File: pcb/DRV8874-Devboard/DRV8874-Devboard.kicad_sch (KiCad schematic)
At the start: 8 parts, among them J1 Conn_01x04_Pin, J2 Screw_Terminal_01x02, J3 Conn_01x03_Pin, U1 DRV8874

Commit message: updated BOM
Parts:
- added C5: 100nF, symbol Device:C
- added U2: TinyThinker_J1, Connector_PinSocket_2.54mm:PinSocket_2x20_P2.54mm_Vertical, symbol Custom_Library:TinyThinker_J1
- added U3: TinyThinker_J2, Connector_PinSocket_2.54mm:PinSocket_2x20_P2.54mm_Vertical, symbol Custom_Library:TinyThinker_J2
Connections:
- net +3.3V: now also U3.1 (+3.3V), U3.10 (+3.3V), U3.18 (+3.3V), U3.2 (+3.3V), U3.21 (+3.3V), U3.22 (+3.3V), U3.29 (+3.3V), U3.30 (+3.3V), U3.38 (+3.3V), U3.9 (+3.3V)
- net +BATT: now also C5.1
- net GND: now also C5.2, U3.16 (GND), U3.19 (GND), U3.20 (GND), U3.27 (GND), U3.28 (GND), U3.36 (GND), U3.39 (GND), U3.40 (GND), U3.7 (GND), U3.8 (GND)
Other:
- moved on the sheet: C1, C2, C3, C4, J3, U1

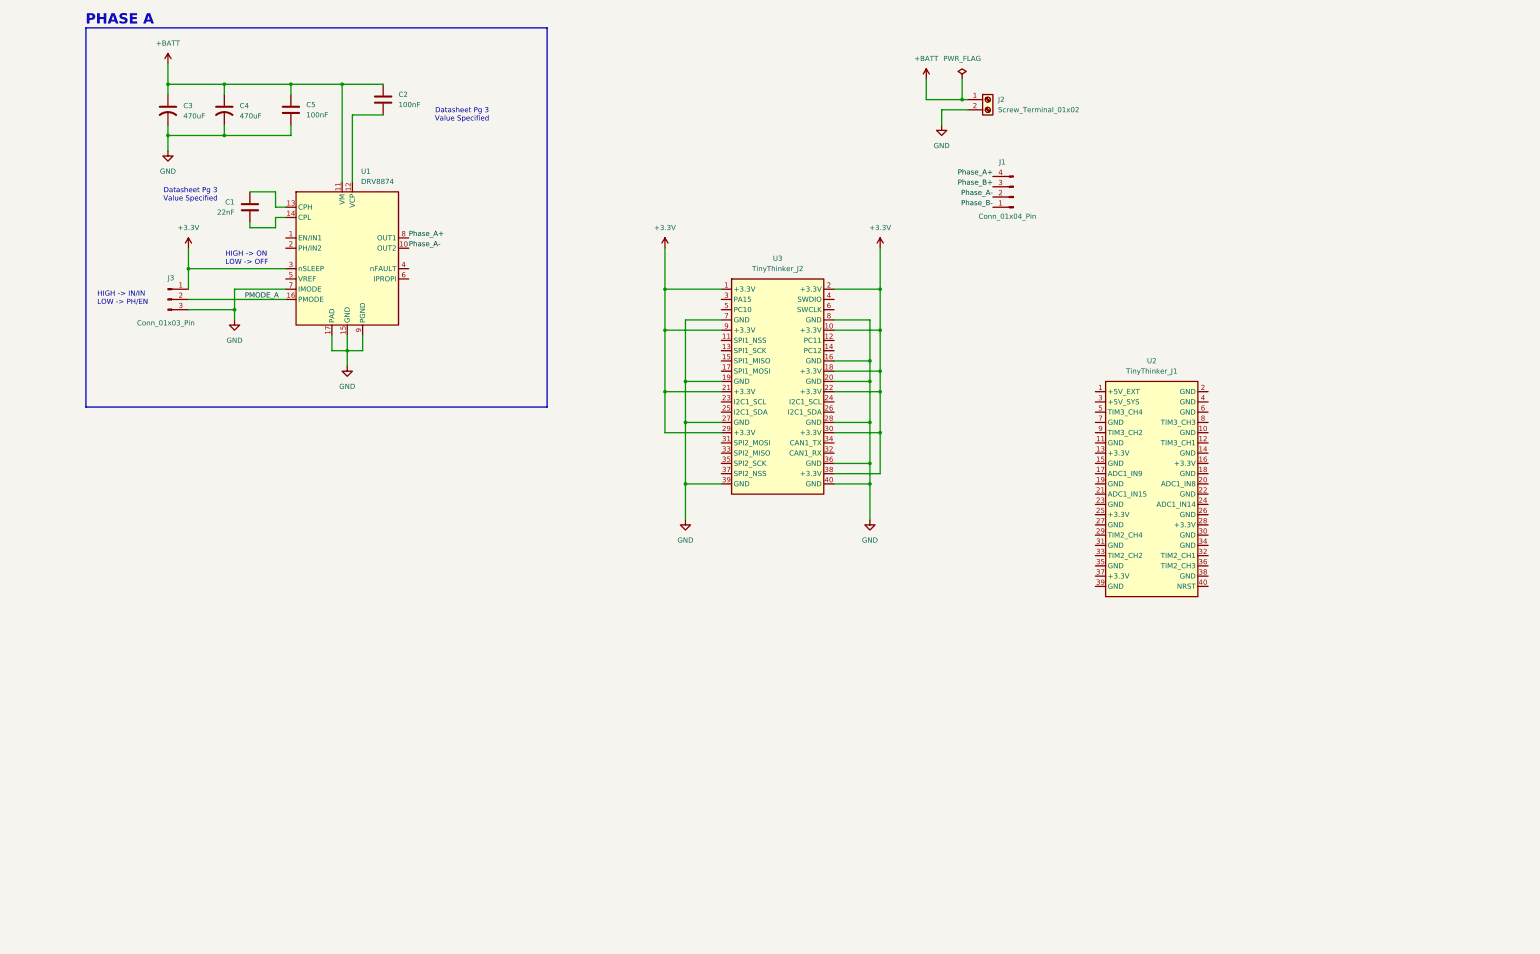
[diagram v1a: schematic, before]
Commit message: added CAN transciever
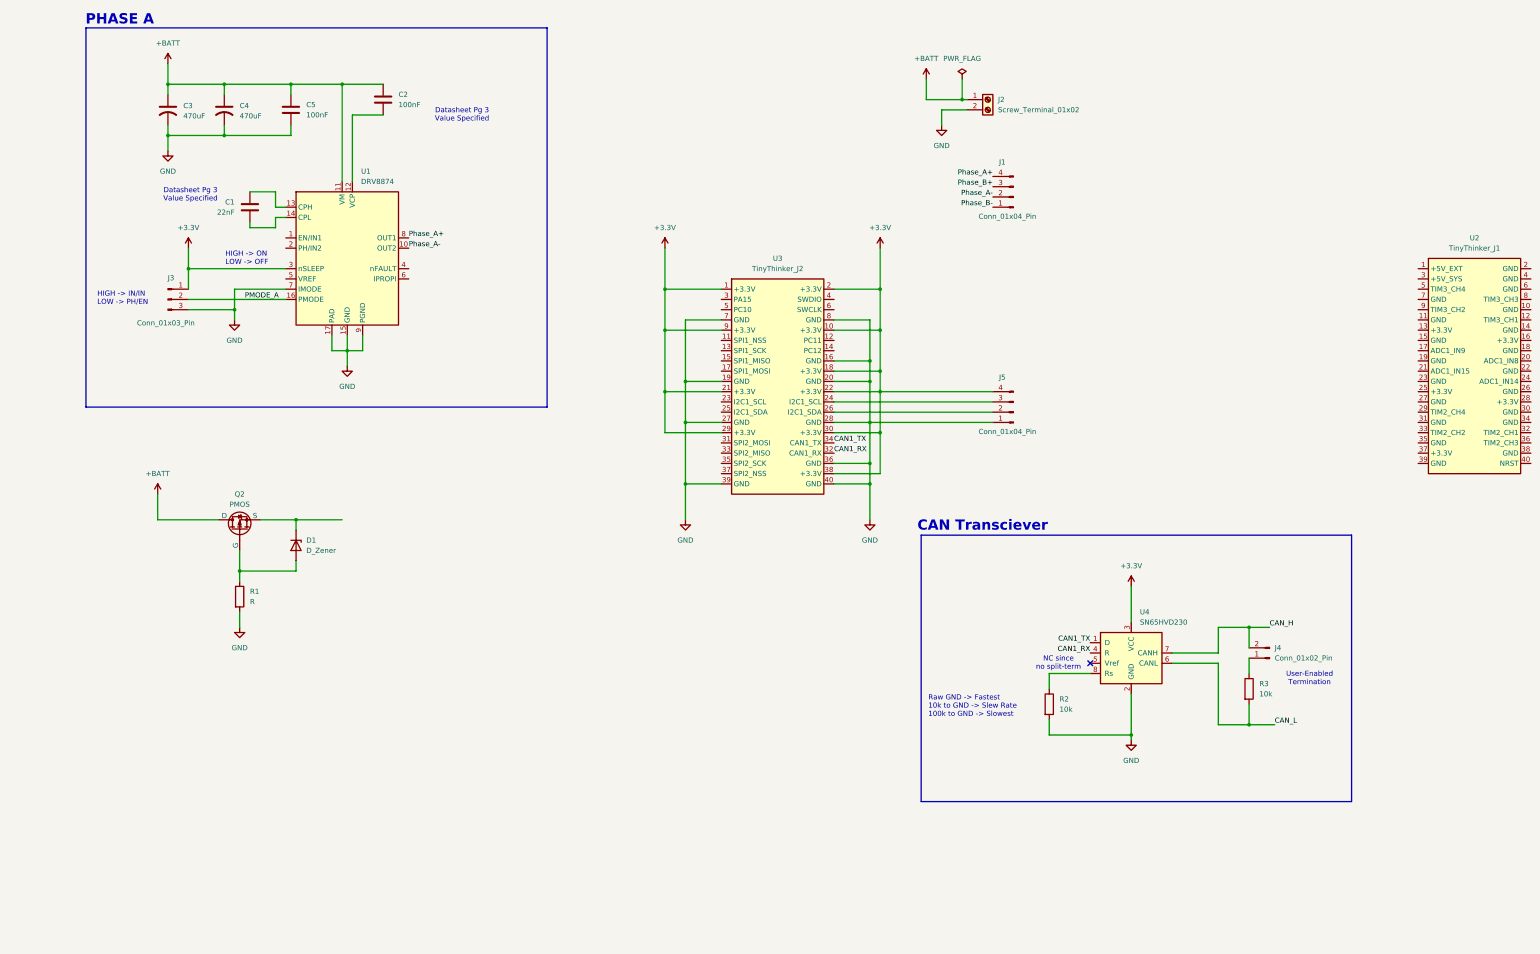
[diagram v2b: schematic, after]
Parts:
- added D1: D_Zener, symbol Device:D_Zener
- added J4: Conn_01x02_Pin, Connector_PinHeader_2.54mm:PinHeader_1x02_P2.54mm_Vertical, symbol Connector:Conn_01x02_Pin
- added J5: Conn_01x04_Pin, symbol Connector:Conn_01x04_Pin
- added Q2: PMOS, symbol Simulation_SPICE:PMOS
- added R1: R, symbol Device:R
- added R2, R3: 10k, symbol Device:R
- added U4: SN65HVD230, Package_SO:SOIC-8_3.9x4.9mm_P1.27mm, symbol Interface_CAN_LIN:SN65HVD230
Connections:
- net +3.3V: now also J5.4 (Pin_4), U4.3 (VCC)
- net +BATT: now also Q2.1 (D)
- net GND: now also J5.1 (Pin_1), R1.2, R2.2, U4.2 (GND)
- net at U3.24 (I2C1_SCL): now also J5.3 (Pin_3)
- net at U3.26 (I2C1_SDA): now also J5.2 (Pin_2)
- net CAN1_RX: now reaches U3.32 (CAN1_RX)
- net CAN1_RX: now also U4.4 (R)
- net CAN1_TX: now reaches U3.34 (CAN1_TX)
- net CAN1_TX: now also U4.1 (D)
- new net: J4.1 (Pin_1), R3.1
- new net: R2.1, U4.8 (Rs)
- new net: D1.2 (A), Q2.2 (G), R1.1
- new net: D1.1 (K), Q2.3 (S)
- new net CAN_H: J4.2 (Pin_2), U4.7 (CANH)
- new net CAN_L: R3.2, U4.6 (CANL)
- no-connect marks 0 -> 1
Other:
- note added: "CAN Transciever"
- note added: "NC since no split-term"
- note added: "Raw GND -> Fastest 10k to GND -> Slew Rate 100k to GND -> Slowest"
- note added: "User-Enabled Termination"
- moved on the sheet: U2

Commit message: exposed more connectors on DRV8874 devb
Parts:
- removed J4: Conn_01x02_Pin, Connector_PinHeader_2.54mm:PinHeader_1x02_P2.54mm_Vertical, symbol Connector:Conn_01x02_Pin
- added J4, J6, J7: Conn_01x03_Pin, Connector_PinHeader_2.54mm:PinHeader_1x03_P2.54mm_Vertical, symbol Connector:Conn_01x03_Pin
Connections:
- net CAN_H: now also J4.3 (Pin_3), J7.3 (Pin_3)
- net CAN_L: now also J7.1 (Pin_1)
- net GND: now also J6.1 (Pin_1), J7.2 (Pin_2)
- net I2C1_SDA: now reaches J5.2 (Pin_2), U3.26 (I2C1_SDA)
- net I2C1_SCL: now reaches J5.3 (Pin_3), U3.24 (I2C1_SCL)
- net at R3.1: now also J4.2 (Pin_2)
- net at U4.8 (Rs): now also J6.2 (Pin_2); no longer R2.1
- new net: J6.3 (Pin_3), R2.1
- no-connect marks 1 -> 4
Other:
- note added: "3 pin to hold jumper"
- note added: "CAN Connector"
- note added: "I2C Connector"
- note added: "Jumper to control speed"
- note added: "Stepper Connector"
- moved on the sheet: J1, R2, R3, U2, U4

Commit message: started working on drv8874
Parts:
- added U5: DRV8841PWP, DRV8841PWP:IC_TPS61196PWPRQ1, symbol DRV8841PWP:DRV8841PWP
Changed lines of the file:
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@@
+	)
+	(symbol
+		(lib_id "DRV8841PWP:DRV8841PWP")
+		(at 181.61 214.63 0)
+		(unit 1)
+		(exclude_from_sim no)
+		(in_bom yes)
+		(on_board yes)
+		(dnp no)
+		(fields_autoplaced yes)
+		(property "Reference" "U5"
+			(at 181.61 173.99 0)
+			(effects
+				(font
+					(size 1.27 1.27)
+				)
+			)
+		)
+		(property "Value" "DRV8841PWP"
+			(at 181.61 176.53 0)
+			(effects
+				(font
+					(size 1.27 1.27)
+				)
+			)
+		)
+		(property "Footprint" "DRV8841PWP:IC_TPS61196PWPRQ1"
+			(at 181.61 214.63 0)
+			(effects
+				(font
+					(size 1.27 1.27)
+				)
+				(justify bottom)
+				(hide yes)
+			)
+		)
+		(property "Datasheet" ""
+			(at 181.61 214.63 0)
+			(effects
+				(font
+					(size 1.27 1.27)
+				)
+				(hide yes)
+			)
+		)
+		(property "Description" ""
+			(at 181.61 214.63 0)
+			(effects
+				(font
+					(size 1.27 1.27)
+				)
+				(hide yes)
+			)
+		)
+		(property "MF" "Texas Instruments"
+			(at 181.61 214.63 0)
+			(effects
+				(font
+					(size 1.27 1.27)
+				)
+				(justify bottom)
+				(hide yes)
+			)
+		)
+		(property "Description_1" "45-V, 2.5-A bipolar stepper or dual H-bridge motor driver IC with current regulation and PWM control"
+			(at 181.61 214.63 0)
+			(effects
+				(font
+					(size 1.27 1.27)
+				)
+				(justify bottom)
+				(hide yes)
+			)
+		)
+		(property "Package" "HTSSOP-28 Texas Instruments"
+			(at 181.61 214.63 0)
+			(effects
+				(font
+					(size 1.27 1.27)
+				)
+				(justify bottom)
+				(hide yes)
+			)
+		)
+		(property "Price" "None"
+			(at 181.61 214.63 0)
+			(effects
+				(font
+					(size 1.27 1.27)
+				)
+				(justify bottom)
+				(hide yes)
+			)
+		)
+		(property "SnapEDA_Link" "https://www.snapeda.com/parts/DRV8841PWP/Texas+Instruments/view-part/?ref=snap"
+			(at 181.61 214.63 0)
+			(effects
+				(font
+					(size 1.27 1.27)
+				)
+				(justify bottom)
+				(hide yes)
+			)
+		)
+		(property "MP" "DRV8841PWP"
+			(at 181.61 214.63 0)
+			(effects
+				(font
+					(size 1.27 1.27)
+				)
+				(justify bottom)
+				(hide yes)
+			)
+		)
+		(property "Availability" "In Stock"
+			(at 181.61 214.63 0)
+			(effects
+				(font
+					(size 1.27 1.27)
+				)
+				(justify bottom)
+				(hide yes)
+			)
+		)
+		(property "Check_prices" "https://www.snapeda.com/parts/DRV8841PWP/Texas+Instruments/view-part/?ref=eda"
+			(at 181.61 214.63 0)
+			(effects
+				(font
+					(size 1.27 1.27)
+				)
+				(justify bottom)
+				(hide yes)
+			)
+		)
+		(pin "4"
+		)
+		(pin "1"
+		)
+		(pin "17"
+		)
+		(pin "10"
+		)
+		(pin "15"
+		)
+		(pin "19"
+		)
+		(pin "28"
+		)
+		(pin "11"
+		)
+		(pin "27"
+		)
+		(pin "21"
+		)
+		(pin "25"
+		)
+		(pin "12"
+		)
+		(pin "9"
+		)
+		(pin "22"
+		)
+		(pin "8"
+		)
+		(pin "23"
+		)
+		(pin "5"
+		)
+		(pin "6"
+		)
+		(pin "24"
+		)
+		(pin "20"
+		)
+		(pin "7"
+		)
+		(pin "16"
+		)
+		(pin "18"
+		)
+		(pin "2"
+		)
+		(pin "26"
+		)
+		(pin "14"
+		)
+		(pin "3"
+		)
+		(pin "13"
+		)
+		(instances
+			(project ""
+				(path "/b57ce88b-13b6-41b4-aa44-cbc2ef4083a9"
+					(reference "U5")
+					(unit 1)
+				)
+			)
+		)
 	)
 	(symbol

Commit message: minor changes to DRV8874
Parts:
- removed D1: D_Zener, symbol Device:D_Zener
- removed Q2: PMOS, symbol Simulation_SPICE:PMOS
- removed R1: R, symbol Device:R
- removed U5: DRV8841PWP, DRV8841PWP:IC_TPS61196PWPRQ1, symbol DRV8841PWP:DRV8841PWP
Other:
- moved on the sheet: U2

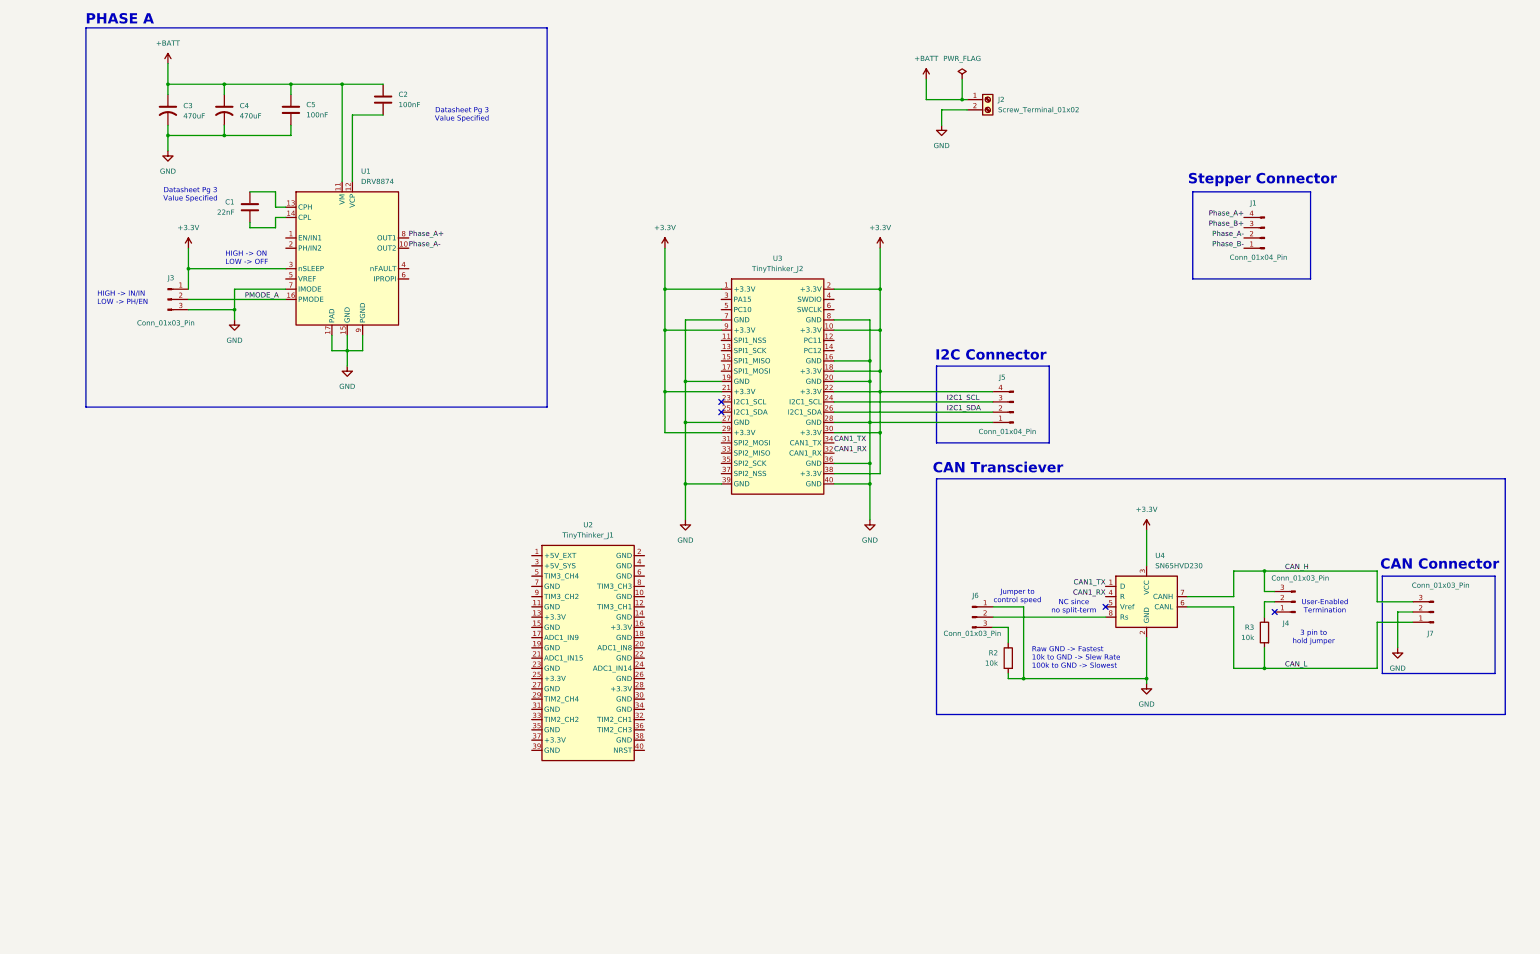
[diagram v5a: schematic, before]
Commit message: worked on DRV8874
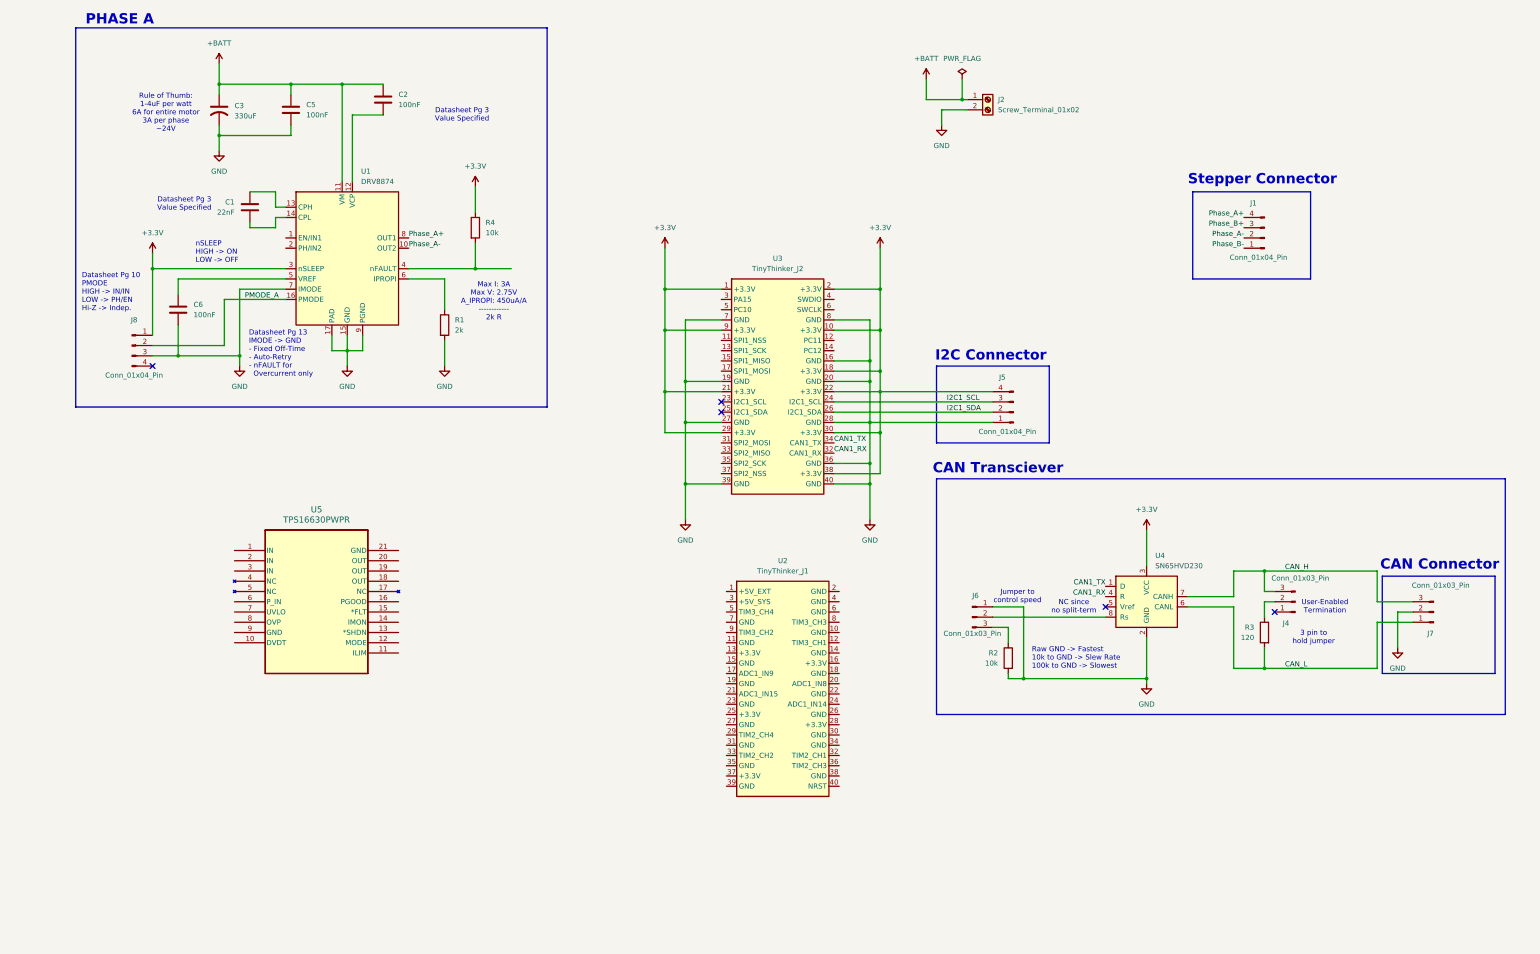
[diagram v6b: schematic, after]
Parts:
- removed C4: 470uF, Custom_Library:CAP-SMD_BD12.5-L13.5-W13.5-RD, symbol Device:C_US
- removed J3: Conn_01x03_Pin, Connector_PinHeader_2.54mm:PinHeader_1x03_P2.54mm_Vertical, symbol Connector:Conn_01x03_Pin
- added C6: 100nF, symbol Device:C
- added J8: Conn_01x04_Pin, symbol Connector:Conn_01x04_Pin
- added R1: 2k, symbol Device:R
- added R4: 10k, symbol Device:R
- added U5: TPS16630PWPR, HTSSOP20_PWP_TEX, symbol Custom_Library:TPS16630PWPR
- C3: value 470uF -> 330uF; footprint Custom_Library:CAP-SMD_BD12.5-L13.5-W13.5-RD -> Capacitor_SMD:CP_Elec_10x10.5; JLCPCB Part # C90272 -> C3032175
- R3: value 10k -> 120
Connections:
- net +3.3V: now also J8.1 (Pin_1), R4.1
- net GND: now also C6.2, J8.3 (Pin_3), R1.2
- net PMODE_A: now also J8.2 (Pin_2)
- net at U1.4 (nFAULT): now also R4.2
- net at U1.5 (VREF): now also C6.1
- net at U1.6 (IPROPI): now also R1.1
- no-connect marks 4 -> 5
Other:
- note added: "Datasheet Pg 10 PMODE HIGH -> IN/IN LOW -> PH/EN Hi-Z -> Indep."
- note added: "Datasheet Pg 13 IMODE -> GND - Fixed Off-Time - Auto-Retry - nFAULT for Overcurrent only"
- note added: "Max I: 3A Max V: 2.75V A_IPROPI: 450uA/A ------------ 2k R"
- note added: "Rule of Thumb: 1-4uF per watt 6A for entire motor 3A per phase ~24V"
- note added: "nSLEEP HIGH -> ON LOW -> OFF"
- note removed: "HIGH -> IN/IN LOW -> PH/EN"
- note removed: "HIGH -> ON LOW -> OFF"
- moved on the sheet: C3, U2

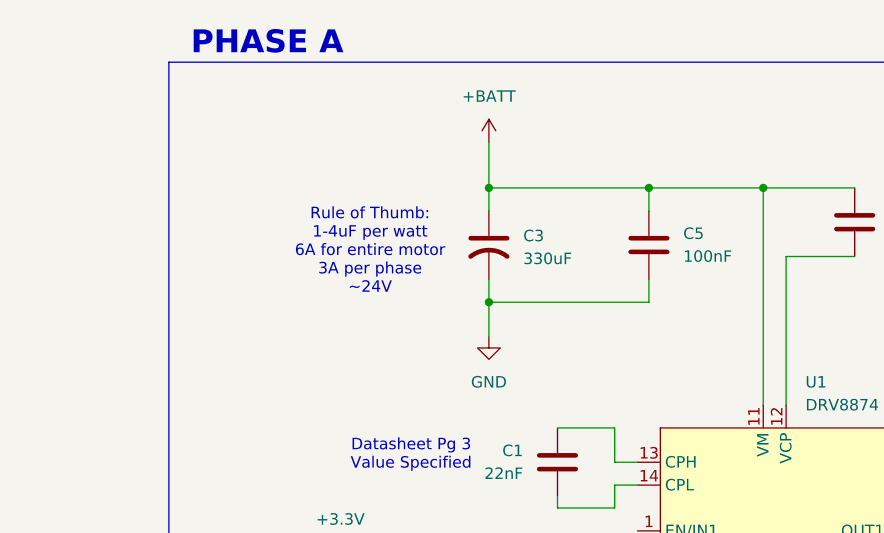
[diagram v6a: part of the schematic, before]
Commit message: Update DRV8874-Devboard.kicad_sch
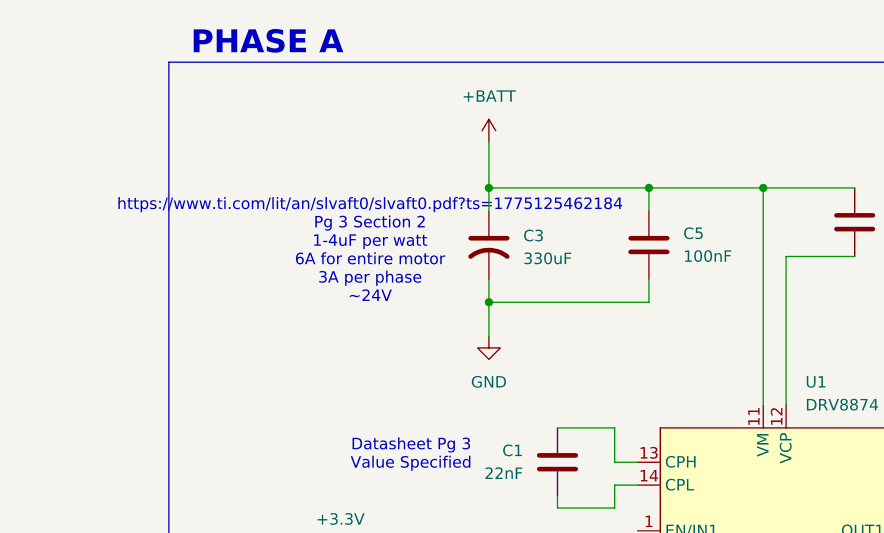
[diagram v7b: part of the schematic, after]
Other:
- note added: "https://www.ti.com/lit/an/slvaft0/slvaft0.pdf?ts=1775125462184 Pg 3 Section 2 1-4uF per watt 6A for entire motor 3A per phase ~24V"
- note removed: "Rule of Thumb: 1-4uF per watt 6A for entire motor 3A per phase ~24V"
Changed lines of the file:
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@@
 		)
 	)
-	(text "Rule of Thumb:\n1-4uF per watt\n6A for entire motor\n3A per phase\n~24V"
+	(text "https://www.ti.com/lit/an/slvaft0/slvaft0.pdf?ts=1775125462184\nPg 3 Section 2\n1-4uF per watt\n6A for entire motor\n3A per phase\n~24V"
 		(exclude_from_sim no)
 		(at 41.402 43.942 0)
